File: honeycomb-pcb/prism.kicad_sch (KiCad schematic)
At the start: 8 parts, among them J501 FFC_P1mm_BOT_RA_SMD, U501 MAX13431E

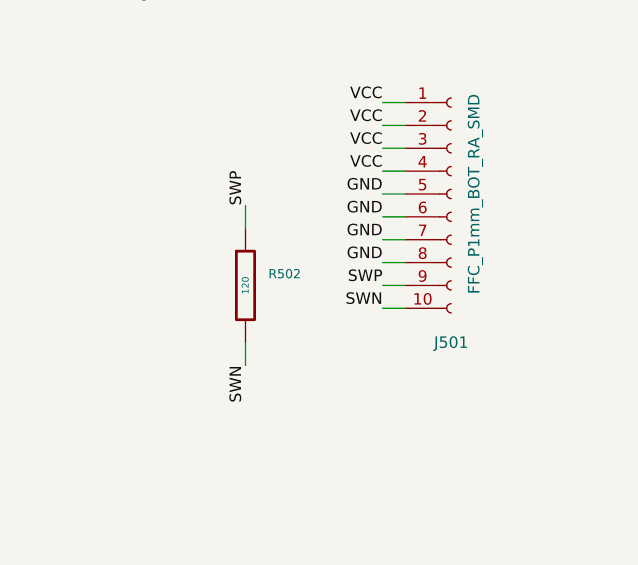
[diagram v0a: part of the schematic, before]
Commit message: motor -> prism
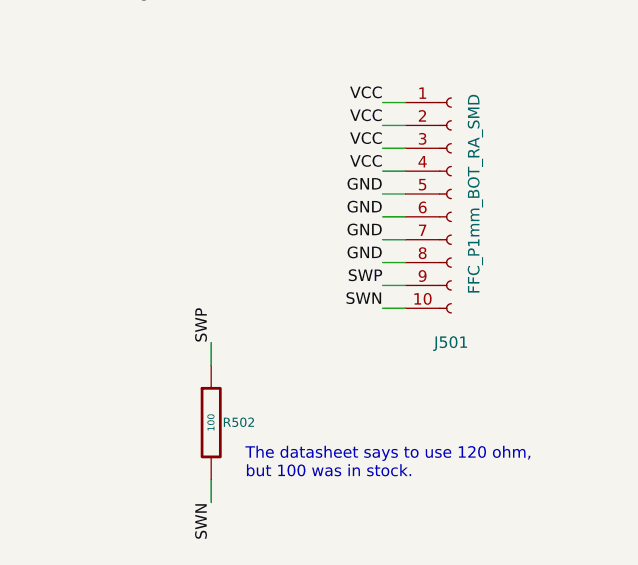
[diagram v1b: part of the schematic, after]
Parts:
- removed R502: 120, Janelia:R_0402_1005Metric, symbol Janelia:R_120_0402
- added R502: 100, Janelia:R_0402_1005Metric, symbol Janelia:R_100_0402
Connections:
- net SWN: now also R502.2
- net SWP: now also R502.1
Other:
- note added: "The datasheet says to use 120 ohm, but 100 was in stock."
- company: (none) -> Howard Hughes Medical Institute
- title: (none) -> honeycomb-pcb
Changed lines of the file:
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@@
 (kicad_sch (version 20230121) (generator eeschema)
   (paper "A4")
+  (title_block
+    (title "honeycomb-pcb")
+    (date "2024-07-12")
+    (rev "1.0")
+    (company "Howard Hughes Medical Institute")
+  )
   (wire (pts (xy 128.27 95.25) (xy 130.81 95.25))
     (stroke (width 0) (type default))
@@
     (stroke (width 0) (type default))
   )
-  (wire (pts (xy 198.12 113.03) (xy 198.12 115.57))
+  (wire (pts (xy 194.31 128.27) (xy 194.31 130.81))
     (stroke (width 0) (type default))
   )
@@
     (stroke (width 0) (type default))
   )
-  (wire (pts (xy 198.12 100.33) (xy 198.12 97.79))
+  (wire (pts (xy 194.31 115.57) (xy 194.31 113.03))
     (stroke (width 0) (type default))
   )
@@
     (stroke (width 0) (type default))
   )
+  (text "The datasheet says to use 120 ohm,\nbut 100 was in stock.\n"
+    (at 198.12 128.27 0)
+    (effects (font (size 1.27 1.27)) (justify left bottom))
+  )
   (label "SWN" (at 153.67 90.17 0) (fields_autoplaced)
     (effects (font (size 1.27 1.27)) (justify left bottom))
@@
     (effects (font (size 1.27 1.27)) (justify right bottom))
   )
-  (label "SWN" (at 198.12 115.57 270) (fields_autoplaced)
+  (label "SWN" (at 194.31 130.81 270) (fields_autoplaced)
     (effects (font (size 1.27 1.27)) (justify right bottom))
   )
@@
     (effects (font (size 1.27 1.27)) (justify right bottom))
   )
-  (label "SWP" (at 198.12 97.79 90) (fields_autoplaced)
+  (label "SWP" (at 194.31 113.03 90) (fields_autoplaced)
     (effects (font (size 1.27 1.27)) (justify left bottom))
   )
@@
     )
   )
-  (symbol (lib_id "Janelia:R_120_0402") (at 198.12 106.68 0) (unit 1)
-    (in_bom yes) (on_board yes) (dnp no) (fields_autoplaced)
-    (property "Reference" "R502" (at 200.66 105.41 0)
+  (symbol (lib_id "Janelia:R_100_0402") (at 194.31 121.92 0) (unit 1)
+    (in_bom yes) (on_board yes) (dnp no)
+    (property "Reference" "R502" (at 195.58 121.92 0)
       (effects (font (size 1.016 1.016)) (justify left))
     )
-    (property "Value" "120" (at 198.12 106.68 90) (do_not_autoplace)
+    (property "Value" "100" (at 194.31 121.92 90)
       (effects (font (size 0.762 0.762)))
     )
-    (property "Footprint" "Janelia:R_0402_1005Metric" (at 196.342 106.68 90)
+    (property "Footprint" "Janelia:R_0402_1005Metric" (at 192.532 121.92 90)
       (effects (font (size 0.762 0.762)) hide)
     )
-    (property "Datasheet" "" (at 200.152 106.68 90)
+    (property "Datasheet" "" (at 196.342 121.92 90)
       (effects (font (size 0.762 0.762)))
     )
-    (property "Vendor" "JLCPCB" (at 202.692 104.14 90)
-      (effects (font (size 1.524 1.524)) hide)
-    )
-    (property "Vendor Part Number" "C432822" (at 205.232 101.6 90)
-      (effects (font (size 1.524 1.524)) hide)
-    )
-    (property "Synopsis" "RES SMD 120 OHM 1% 62.5mW" (at 207.772 99.06 90)
-      (effects (font (size 1.524 1.524)) hide)
-    )
-    (property "Package" "0402" (at 198.12 106.68 0)
-      (effects (font (size 1.27 1.27)) hide)
-    )
-    (property "Manufacturer" "TA-I Tech" (at 198.12 106.68 0)
-      (effects (font (size 1.27 1.27)) hide)
-    )
-    (property "Manufacturer Part Number" "RM04FTN1200" (at 198.12 106.68 0)
-      (effects (font (size 1.27 1.27)) hide)
-    )
-    (property "LCSC" "C432822" (at 198.12 106.68 0)
-      (effects (font (size 1.27 1.27)) hide)
-    )
+    (property "Vendor" "JLCPCB" (at 198.882 119.38 90)
+      (effects (font (size 1.524 1.524)) hide)
+    )
+    (property "Vendor Part Number" "C25076" (at 201.422 116.84 90)
+      (effects (font (size 1.524 1.524)) hide)
+    )
+    (property "Synopsis" "RES SMD 100 OHM 1% 62.5mW" (at 203.962 114.3 90)
+      (effects (font (size 1.524 1.524)) hide)
+    )
+    (property "Package" "0402" (at 194.31 121.92 0)
+      (effects (font (size 1.27 1.27)) hide)
+    )
+    (property "Manufacturer" "UNI-ROYAL(Uniroyal Elec)" (at 194.31 121.92 0)
+      (effects (font (size 1.27 1.27)) hide)
+    )
+    (property "Manufacturer Part Number" "0402WGF1000TCE" (at 194.31 121.92 0)
+      (effects (font (size 1.27 1.27)) hide)
+    )
+    (property "LCSC" "C25076" (at 194.31 121.92 0)
+      (effects (font (size 1.27 1.27)) hide)
+    )
+    (pin "1")
     (pin "2")
-    (pin "1")
     (instances
       (project "honeycomb-pcb"

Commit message: Update BOM
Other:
- note added: "Convert 48V down to ~46V."
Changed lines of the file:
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@@
   (title_block
     (title "honeycomb-pcb")
-    (date "2024-07-12")
+    (date "2024-07-16")
     (rev "1.0")
     (company "Howard Hughes Medical Institute")
@@
     (effects (font (size 1.27 1.27)) (justify left bottom))
   )
+  (text "Convert 48V down to ~46V.\n" (at 196.85 50.8 0)
+    (effects (font (size 1.27 1.27)) (justify left bottom))
+  )

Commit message: Last update before renaming
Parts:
- U501: Package (none) -> TDFN-10-EP(3x3)
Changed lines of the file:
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@@
+      (effects (font (size 1.27 1.27)) hide)
+    )
+    (property "Package" "TDFN-10-EP(3x3)" (at 140.97 92.71 0)
       (effects (font (size 1.27 1.27)) hide)
     )
